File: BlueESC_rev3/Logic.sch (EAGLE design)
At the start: 77 parts, among them Q1 BC817-40W, Q2 BC817-40W, Q3 BC817-40W, Q4 SI7370, Q5 SI7370, Q6 SI7370, Q7 SI7370, Q8 SI7370, Q9 SI7370, U1 ATMEGA168MLF, U2 V_REG_LDOSMD, Y1 RESONATORSMD

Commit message: Updated rev3 schematic and split the schematic into two boards.
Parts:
- added C11: 47uF, SparkFun-Capacitors:CAP_POL7343
- added JP1, JP3: (no value), SparkFun-Connectors:M05PTH
- added JP2: (no value), SparkFun-Connectors:M081X08
- added R20: 3.3K, SparkFun-Resistors:33KOHM1/10W1%(0603)
- added R33: 10K, SparkFun-Resistors:33KOHM1/10W1%(0603)
- C15, C16, C17: value 33uF -> 47uF; device SparkFun-Capacitors:CAP_POL6032 -> SparkFun-Capacitors:CAP_POL7343
- LED1, LED2: device SparkFun:LED-3MM-NO_SILK -> SparkFun:LED0603
- R10: value 10K -> 18K 1%
- R11: value 1K -> 3.3K 1%
- U$1, U$2: value PAD2X3MM -> PADPTH-MED; device BR-Eagle-Library:PAD2X3MM -> BR-Eagle-Library:PADPTH-MED
- U1: value ATMEGA168MLF -> ATMEGA168; device SparkFun-DigitalIC:ATMEGA168MLF -> SparkFun-DigitalIC:ATMEGA168
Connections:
- net CURRENT_ADC: now also JP3.2
- net GND: now also C11.-, JP1.1, JP1.5, JP2.1, JP2.8, JP3.5, R33.1
- net PHASE_A: now also JP1.2
- net PHASE_B: now also JP1.3
- net PHASE_C: now also JP1.4
- net PWM_AH: now also JP2.2
- net PWM_AL: now also JP2.3
- net PWM_BH: now also JP2.4
- net PWM_BL: now also JP2.5
- net PWM_CH: now also JP2.6
- net PWM_CL: now also JP2.7
- net TEMP_ADC: now also JP3.1, R20.1, R33.2
- net VBAT: now also C11.+, JP3.3
- net VBAT_ADC: no longer C4.1
- net VCC5V: now also C4.1, JP3.4, R20.2
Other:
- note added: "BOTTOM BOARD"
- note added: "Current Sense"
- note added: "Interface between top and bottom board (ignore for now)"
- note added: "MIC5235 - 150mA - 24Vin"
- note added: "TOP BOARD"
- note added: "Temperature Sense"
- moved on the sheet: C10, C15, C16, C17, C4, C8, R1, R2, R3, R4, R5, R6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

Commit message: Rev3 (two boards) laid out and ready to go. Final review may create a few changes.
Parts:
- removed C1, C2, C3: 1uF, SparkFun-Capacitors:CAP0805
- removed C10, C6, C8: 0.1uF, SparkFun-Capacitors:CAP0603-CAP
- removed C11, C15, C16, C17: 47uF, SparkFun-Capacitors:CAP_POL7343
- removed D1, D2, D3: Schottky, SparkFun-DiscreteSemi:DIODESOD
- removed JP1, JP3: (no value), SparkFun-Connectors:M05PTH
- removed JP2: (no value), SparkFun-Connectors:M081X08
- removed Q1, Q2, Q3: BC817-40W, SparkFun-DiscreteSemi:TRANSISTOR_NPNSOT23
- removed Q4, Q5, Q6, Q7, Q8, Q9: SI7370, transistor-fet-bobstarr:SI7370
- removed R17, R23, R28: 2.2K, SparkFun-Resistors:33KOHM1/10W1%(0603)
- removed R18, R24, R29: 4.7K, SparkFun-Resistors:33KOHM1/10W1%(0603)
- removed R19, R21, R25, R26, R30, R31: 100, SparkFun-Resistors:33KOHM1/10W1%(0603)
- removed R20: 3.3K, SparkFun-Resistors:33KOHM1/10W1%(0603)
- removed R22, R27, R32, R33: 10K, SparkFun-Resistors:33KOHM1/10W1%(0603)
- removed U$1, U$2: PADPTH-MED, BR-Eagle-Library:PADPTH-MED
- removed U$15: ACS712, SparkFun-AnalogIC:ACS712
- removed U$5, U$6, U$7: PAD2X3MM, BR-Eagle-Library:PAD2X3MM
- added U$16: HEADER-62MM, BR-Eagle-Library:HEADER-62MM
- added U$17: HEADER-122MM, BR-Eagle-Library:HEADER-122MM
- LED1: value Yellow -> RED
- LED2: value Green -> BLUE
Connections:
- removed net GATE_AH: Q4.G, R19.2
- removed net GATE_AL: Q5.G, R21.2, R22.2
- removed net GATE_BH: Q6.G, R25.2
- removed net GATE_BL: Q7.G, R26.2, R27.2
- removed net GATE_CH: Q8.G, R30.2
- removed net GATE_CL: Q9.G, R31.2, R32.2
- removed net N$1: C8.1, U$15.FILT
- removed net N$12: C3.1, D1.C, R17.2
- removed net N$15: C1.1, D2.C, R23.2
- removed net N$19: C2.1, D3.C, R28.2
- removed net N$2: Q1.B, R18.2
- removed net N$4: Q1.C, R17.1, R19.1
- removed net N$5: Q2.B, R24.2
- removed net N$6: Q2.C, R23.1, R25.1
- removed net N$7: Q3.B, R29.2
- removed net N$8: C6.1, U1.AREF
- removed net N$9: Q3.C, R28.1, R30.1
- removed net VBAT+: U$1.PAD, U$15.IP+@1, U$15.IP+@2
- net CURRENT_ADC: now also U$17.4, U1.PC3(ADC3); no longer JP3.2, U$15.VOUT, U1.ADC6
- net GND: now also U$16.1, U$17.1, U$17.12, U$17.2; no longer C10.2, C11.-, C15.-, C16.-, C17.-, C6.2, C8.2, JP1.1, JP1.5, JP2.1, JP2.8, JP3.5, Q1.E, Q2.E, Q3.E, Q5.S3, Q7.S3, Q9.S3, R22.1, R27.1, R32.1, R33.1, U$15.GND, U$2.PAD
- net LED_STATUS: now also U1.PB2(SS/OC1B); no longer U1.PD7(AIN1)
- net LED_WARN: now also U1.PB1(OC1A); no longer U1.PD2(INT0)
- net PHASE_A: now also U$16.2; no longer C3.2, JP1.2, Q4.S3, Q5.D, U$5.PAD
- net PHASE_B: now also U$16.3; no longer C1.2, JP1.3, Q6.S3, Q7.D, U$6.PAD
- net PHASE_C: now also U$16.4; no longer C2.2, JP1.4, Q8.S3, Q9.D, U$7.PAD
- net PWM_AH: now also U$17.5, U1.PD2(INT0); no longer JP2.2, R18.1, U$14.MOSI, U1.PB3(MOSI/OC2)
- net PWM_AL: now also U$17.6; no longer JP2.3, R21.1
- net PWM_BH: now also U$17.7, U1.PD4(XCK/T0); no longer JP2.4, R24.1, U1.PB2(SS/OC1B)
- net PWM_BL: now also U$17.8, U1.PD5(T1); no longer JP2.5, R26.1, U1.PD4(XCK/T0)
- net PWM_CH: now also U$17.9, U1.PD7(AIN1); no longer JP2.6, R29.1, U1.PB1(OC1A)
- net PWM_CL: now also U$14.MOSI, U$17.10, U1.PB3(MOSI/OC2); no longer JP2.7, R31.1, U1.PD5(T1)
- net TEMP_ADC: now also U$16.5, U1.ADC7; no longer JP3.1, R20.1, R33.2, U1.PC3(ADC3)
- net VBAT: now also U$17.11; no longer C11.+, C15.+, C16.+, C17.+, D1.A, D2.A, D3.A, JP3.3, Q4.D, Q6.D, Q8.D, U$15.IP-@3, U$15.IP-@4, U2.EN
- net VBAT_ADC: now also U1.ADC6; no longer U1.ADC7
- net VCC5V: now also U$16.6, U$17.3, U1.AREF; no longer C10.1, JP3.4, R20.2, U$15.VCC
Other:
- note added: "TPS70950 150 mA 30V input Internal ENable pullup"
- note removed: "BOTTOM BOARD"
- note removed: "Current Sense"
- note removed: "MIC5235 - 150mA - 24Vin"
- note removed: "MOSFET Driving"
- note removed: "MOSFETs"
- note removed: "Motor Pads"
- note removed: "Power Decoupling"
- note removed: "Power Pads"
- note removed: "TOP BOARD"
- note removed: "Temperature Sense"

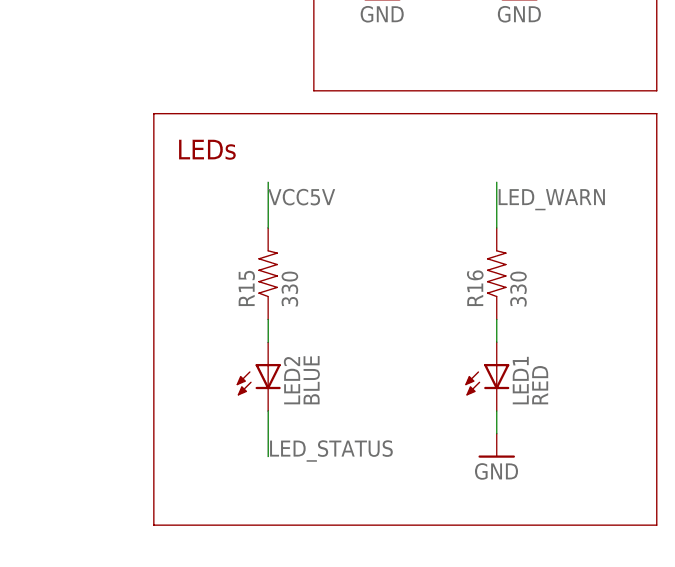
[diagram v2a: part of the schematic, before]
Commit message: Rev 3 changes. Boards have been ordered.
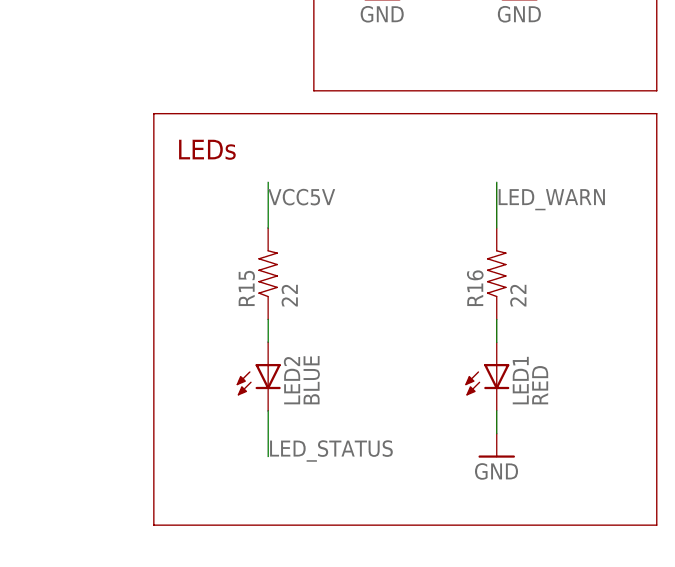
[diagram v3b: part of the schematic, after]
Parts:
- LED1, LED2: device SparkFun:LED0603 -> SparkFun:LED-3MM-NO_SILK
- R15, R16: value 330 -> 22
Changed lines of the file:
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@@
 <grid distance="0.1" unitdist="inch" unit="inch" style="lines" multiple="1" display="no" altdistance="0.01" altunitdist="inch" altunit="inch"/>
 <layers>
-<layer number="1" name="Top" color="4" fill="1" visible="no" active="no"/>
-<layer number="2" name="Route2" color="1" fill="3" visible="no" active="no"/>
-<layer number="3" name="Route3" color="4" fill="3" visible="no" active="no"/>
-<layer number="14" name="Route14" color="1" fill="6" visible="no" active="no"/>
-<layer number="15" name="Route15" color="4" fill="6" visible="no" active="no"/>
-<layer number="16" name="Bottom" color="1" fill="1" visible="no" active="no"/>
-<layer number="17" name="Pads" color="2" fill="1" visible="no" active="no"/>
-<layer number="18" name="Vias" color="2" fill="1" visible="no" active="no"/>
-<layer number="19" name="Unrouted" color="6" fill="1" visible="no" active="no"/>
-<layer number="20" name="Dimension" color="15" fill="1" visible="no" active="no"/>
-<layer number="21" name="tPlace" color="7" fill="1" visible="no" active="no"/>
-<layer number="22" name="bPlace" color="7" fill="1" visible="no" active="no"/>
-<layer number="23" name="tOrigins" color="15" fill="1" visible="no" active="no"/>
-<layer number="24" name="bOrigins" color="15" fill="1" visible="no" active="no"/>
-<layer number="25" name="tNames" color="7" fill="1" visible="no" active="no"/>
-<layer number="26" name="bNames" color="7" fill="1" visible="no" active="no"/>
-<layer number="27" name="tValues" color="7" fill="1" visible="no" active="no"/>
-<layer number="28" name="bValues" color="7" fill="1" visible="no" active="no"/>
+<layer number="1" name="Top" color="4" fill="1" visible="yes" active="no"/>
+<layer number="2" name="Route2" color="1" fill="3" visible="yes" active="no"/>
+<layer number="3" name="Route3" color="4" fill="3" visible="yes" active="no"/>
+<layer number="14" name="Route14" color="1" fill="6" visible="yes" active="no"/>
+<layer number="15" name="Route15" color="4" fill="6" visible="yes" active="no"/>
+<layer number="16" name="Bottom" color="1" fill="1" visible="yes" active="no"/>
+<layer number="17" name="Pads" color="2" fill="1" visible="yes" active="no"/>
+<layer number="18" name="Vias" color="2" fill="1" visible="yes" active="no"/>
+<layer number="19" name="Unrouted" color="6" fill="1" visible="yes" active="no"/>
+<layer number="20" name="Dimension" color="15" fill="1" visible="yes" active="no"/>
+<layer number="21" name="tPlace" color="7" fill="1" visible="yes" active="no"/>
+<layer number="22" name="bPlace" color="7" fill="1" visible="yes" active="no"/>
+<layer number="23" name="tOrigins" color="15" fill="1" visible="yes" active="no"/>
+<layer number="24" name="bOrigins" color="15" fill="1" visible="yes" active="no"/>
+<layer number="25" name="tNames" color="7" fill="1" visible="yes" active="no"/>
+<layer number="26" name="bNames" color="7" fill="1" visible="yes" active="no"/>
+<layer number="27" name="tValues" color="7" fill="1" visible="yes" active="no"/>
+<layer number="28" name="bValues" color="7" fill="1" visible="yes" active="no"/>
 <layer number="29" name="tStop" color="7" fill="3" visible="no" active="no"/>
 <layer number="30" name="bStop" color="7" fill="6" visible="no" active="no"/>
@@
 <layer number="35" name="tGlue" color="7" fill="4" visible="no" active="no"/>
 <layer number="36" name="bGlue" color="7" fill="5" visible="no" active="no"/>
-<layer number="37" name="tTest" color="7" fill="1" visible="no" active="no"/>
-<layer number="38" name="bTest" color="7" fill="1" visible="no" active="no"/>
+<layer number="37" name="tTest" color="7" fill="1" visible="yes" active="no"/>
+<layer number="38" name="bTest" color="7" fill="1" visible="yes" active="no"/>
 <layer number="39" name="tKeepout" color="4" fill="11" visible="no" active="no"/>
 <layer number="40" name="bKeepout" color="1" fill="11" visible="no" active="no"/>
@@
 <layer number="44" name="Drills" color="7" fill="1" visible="no" active="no"/>
 <layer number="45" name="Holes" color="7" fill="1" visible="no" active="no"/>
-<layer number="46" name="Milling" color="3" fill="1" visible="no" active="no"/>
-<layer number="47" name="Measures" color="7" fill="1" visible="no" active="no"/>
-<layer number="48" name="Document" color="7" fill="1" visible="no" active="no"/>
-<layer number="49" name="Reference" color="7" fill="1" visible="no" active="no"/>
-<layer number="50" name="dxf" color="7" fill="1" visible="no" active="no"/>
-<layer number="51" name="tDocu" color="7" fill="1" visible="no" active="no"/>
-<layer number="52" name="bDocu" color="7" fill="1" visible="no" active="no"/>
-<layer number="53" name="tGND_GNDA" color="7" fill="9" visible="no" active="no"/>
-<layer number="54" name="bGND_GNDA" color="1" fill="9" visible="no" active="no"/>
-<layer number="56" name="wert" color="7" fill="1" visible="no" active="no"/>
-<layer number="57" name="tCAD" color="7" fill="1" visible="no" active="no"/>
+<layer number="46" name="Milling" color="3" fill="1" visible="yes" active="no"/>
+<layer number="47" name="Measures" color="7" fill="1" visible="yes" active="no"/>
+<layer number="48" name="Document" color="7" fill="1" visible="yes" active="no"/>
+<layer number="49" name="Reference" color="7" fill="1" visible="yes" active="no"/>
+<layer number="50" name="dxf" color="7" fill="1" visible="yes" active="no"/>
+<layer number="51" name="tDocu" color="7" fill="1" visible="yes" active="no"/>
+<layer number="52" name="bDocu" color="7" fill="1" visible="yes" active="no"/>
+<layer number="53" name="tGND_GNDA" color="7" fill="9" visible="yes" active="no"/>
+<layer number="54" name="bGND_GNDA" color="1" fill="9" visible="yes" active="no"/>
+<layer number="56" name="wert" color="7" fill="1" visible="yes" active="no"/>
+<layer number="57" name="tCAD" color="7" fill="1" visible="yes" active="no"/>
 <layer number="91" name="Nets" color="2" fill="1" visible="yes" active="yes"/>
 <layer number="92" name="Busses" color="1" fill="1" visible="yes" active="yes"/>
@@
 <part name="GND9" library="SparkFun" deviceset="GND" device=""/>
 <part name="Y1" library="SparkFun" deviceset="RESONATOR" device="SMD"/>
-<part name="R15" library="SparkFun" deviceset="RESISTOR" device="0603-RES" value="330"/>
-<part name="LED2" library="SparkFun" deviceset="LED" device="0603" value="BLUE"/>
-<part name="R16" library="SparkFun" deviceset="RESISTOR" device="0603-RES" value="330"/>
-<part name="LED1" library="SparkFun" deviceset="LED" device="0603" value="RED"/>
+<part name="R15" library="SparkFun" deviceset="RESISTOR" device="0603-RES" value="22"/>
+<part name="LED2" library="SparkFun" deviceset="LED" device="-3MM-NO_SILK" value="BLUE"/>
+<part name="R16" library="SparkFun" deviceset="RESISTOR" device="0603-RES" value="22"/>
+<part name="LED1" library="SparkFun" deviceset="LED" device="-3MM-NO_SILK" value="RED"/>
 <part name="GND7" library="SparkFun" deviceset="GND" device=""/>
 <part name="C7" library="SparkFun-Capacitors" deviceset="CAP" device="0603-CAP" value="0.1uF"/>
